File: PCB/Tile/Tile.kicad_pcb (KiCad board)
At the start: 2 copper layers, 100 x 86.6 mm, 40 parts, among them J1 Conn_01x05_Female, U1 HT16K33-28SOP

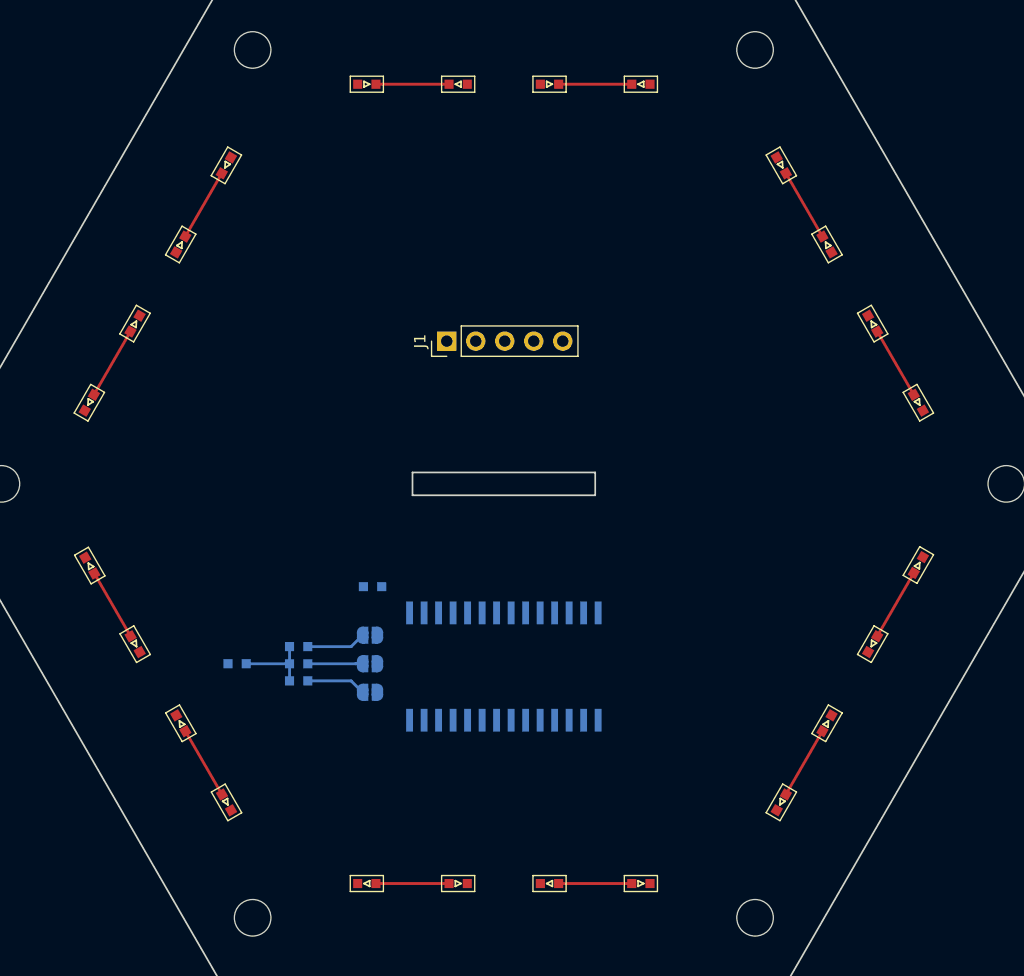
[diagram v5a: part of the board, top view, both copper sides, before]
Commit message: [update] Tileの裏面配線の試行 #3
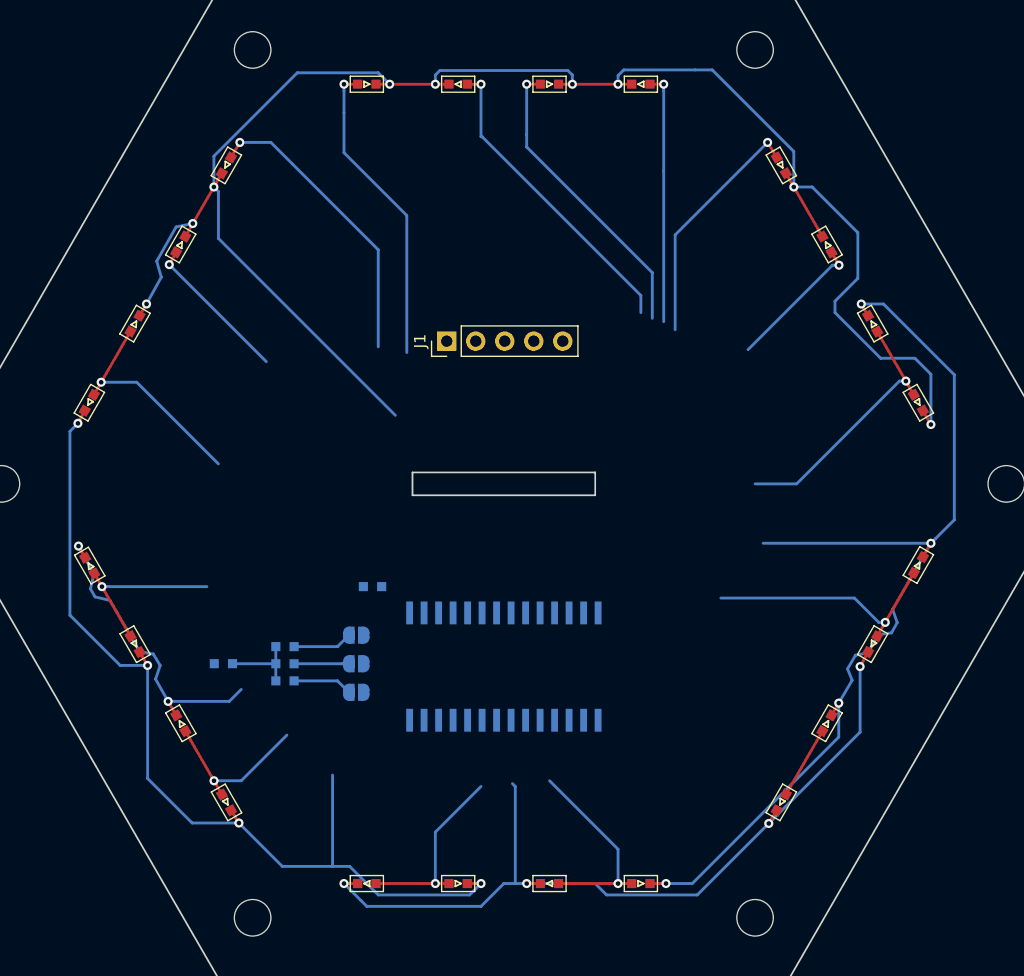
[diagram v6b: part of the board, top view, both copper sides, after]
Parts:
- moved D26 1.20 mm to (105.4, 120.7)
- moved JP1 1.20 mm to (117.1, 123.3)
- moved JP2 1.20 mm to (117.1, 120.8)
- moved JP3 1.20 mm to (117.1, 118.3)
- moved R1 1.20 mm to (110.8, 122.3)
- moved R2 1.20 mm to (110.8, 120.8)
- moved R3 1.20 mm to (110.8, 119.3)
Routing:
- net Net-(D1-Pad1): track 25.6 -> 251.6 mm, vias 0 -> 15
- net Net-(D17-Pad1): track 0.00 -> 170.1 mm, vias 0 -> 8
- net Net-(D13-Pad2): track 0.00 -> 27.1 mm, vias 0 -> 1
- net Net-(D14-Pad2): track 0.00 -> 27.0 mm, vias 0 -> 1
- net Net-(D12-Pad2): track 0.00 -> 26.3 mm, vias 0 -> 1
- net Net-(D15-Pad2): track 0.00 -> 26.0 mm, vias 0 -> 1
- net Net-(D11-Pad2): track 0.00 -> 22.0 mm, vias 0 -> 1
- net Net-(D10-Pad2): track 0.00 -> 21.3 mm, vias 0 -> 1
- net Net-(D24-Pad2): track 6.40 -> 23.3 mm, vias 0 -> 1
- net Net-(D23-Pad2): track 6.40 -> 21.7 mm, vias 0 -> 1
- net Net-(D16-Pad2): track 0.00 -> 13.2 mm, vias 0 -> 1
- net Net-(D1-Pad2): track 6.40 -> 19.6 mm, vias 0 -> 1
- net Net-(D9-Pad2): track 0.00 -> 12.3 mm, vias 0 -> 1
- net Net-(D21-Pad2): track 6.40 -> 17.9 mm, vias 0 -> 1
- net Net-(D20-Pad2): track 6.40 -> 16.6 mm, vias 0 -> 1
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
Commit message: [update] Tileの回路図のピンヘッダの種類を変更 #3
* Tile側のピンヘッダがFemaleになっていたのをMaleに変更
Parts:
- J1: value Conn_01x05_Female -> Conn_01x05_Male
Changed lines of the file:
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@@
       (effects (font (size 1 1) (thickness 0.15)))
     )
-    (fp_text value Conn_01x05_Female (at 0 12.49 90) (layer F.Fab)
+    (fp_text value Conn_01x05_Male (at 0 12.49 90) (layer F.Fab)
       (effects (font (size 1 1) (thickness 0.15)))
     )

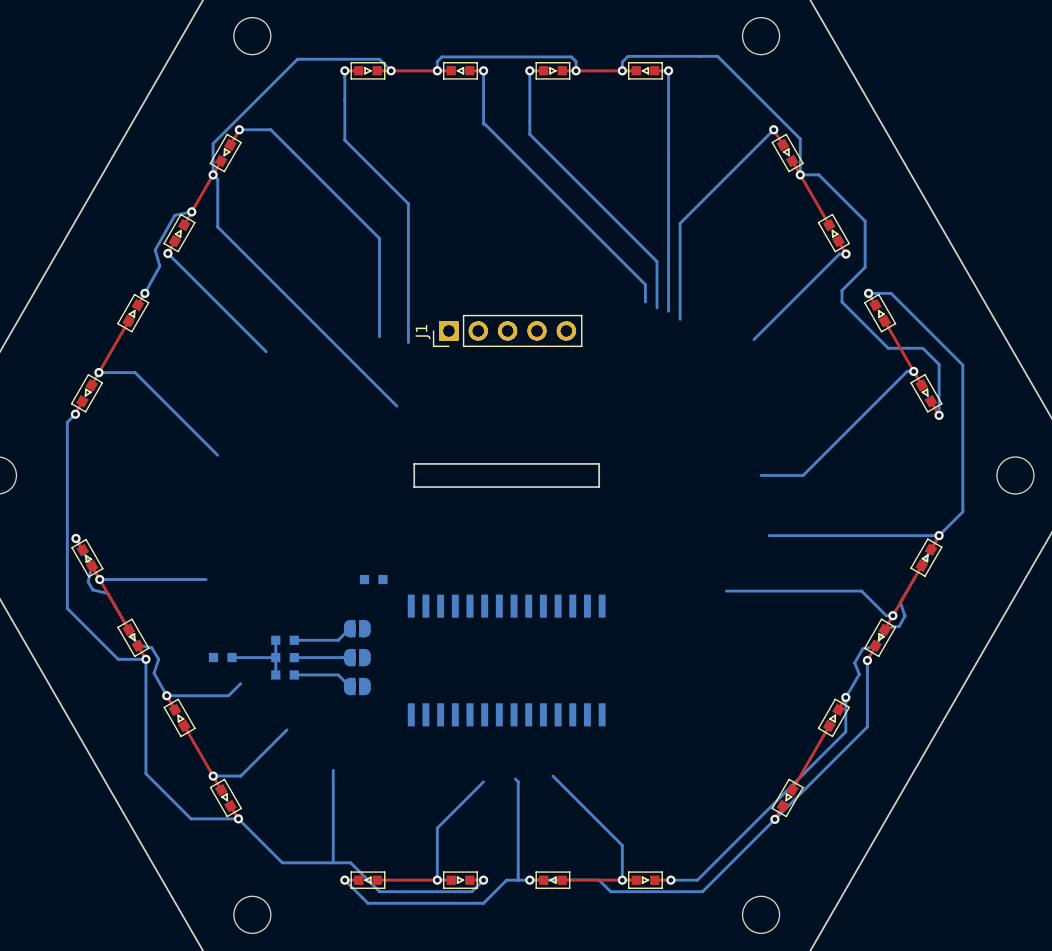
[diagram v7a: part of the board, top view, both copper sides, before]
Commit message: [update] Tileの全LED配線を試作 #3
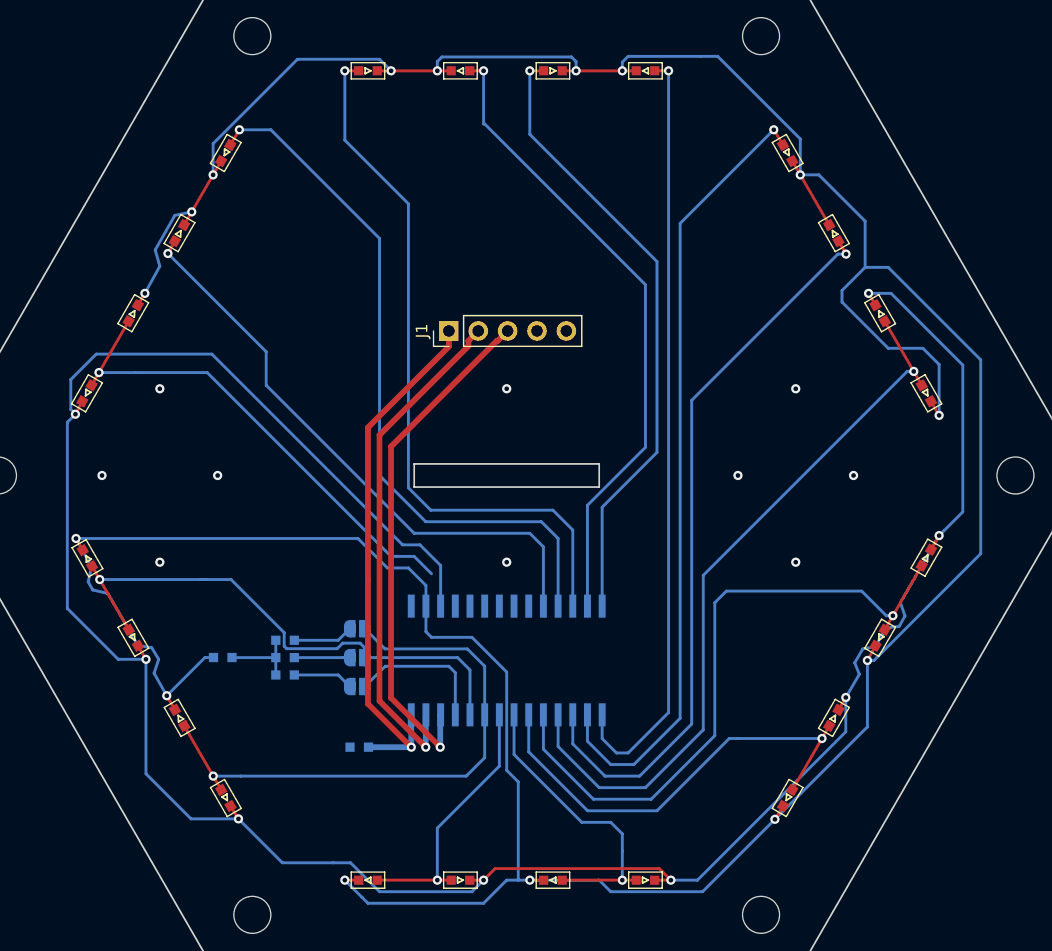
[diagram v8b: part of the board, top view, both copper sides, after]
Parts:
- moved C1 14.6 mm to (117.2, 128.5), turned to 180 degrees
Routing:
- net Net-(D1-Pad1): track 251.6 -> 321.2 mm
- net Net-(D9-Pad2): track 12.3 -> 63.7 mm
- net Net-(D10-Pad2): track 21.3 -> 68.6 mm
- net +5V: track 0.00 -> 47.0 mm, vias 0 -> 1
- net SCL: track 0.00 -> 44.8 mm, vias 0 -> 1
- net Net-(D11-Pad2): track 22.0 -> 66.5 mm
- net SDA: track 0.00 -> 44.0 mm, vias 0 -> 1
- net Net-(D17-Pad1): track 170.1 -> 211.6 mm
- net Net-(D24-Pad2): track 23.3 -> 64.1 mm
- net Net-(D16-Pad2): track 13.2 -> 51.0 mm
- net Net-(D19-Pad2): track 14.4 -> 50.2 mm
- net Net-(D15-Pad2): track 26.0 -> 61.6 mm
- net Net-(D1-Pad2): track 19.6 -> 54.8 mm
- net Net-(D14-Pad2): track 27.0 -> 61.9 mm
- net Net-(D23-Pad2): track 21.7 -> 56.5 mm
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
